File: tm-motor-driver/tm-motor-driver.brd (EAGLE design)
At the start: 47 x 26 mm, 18 parts

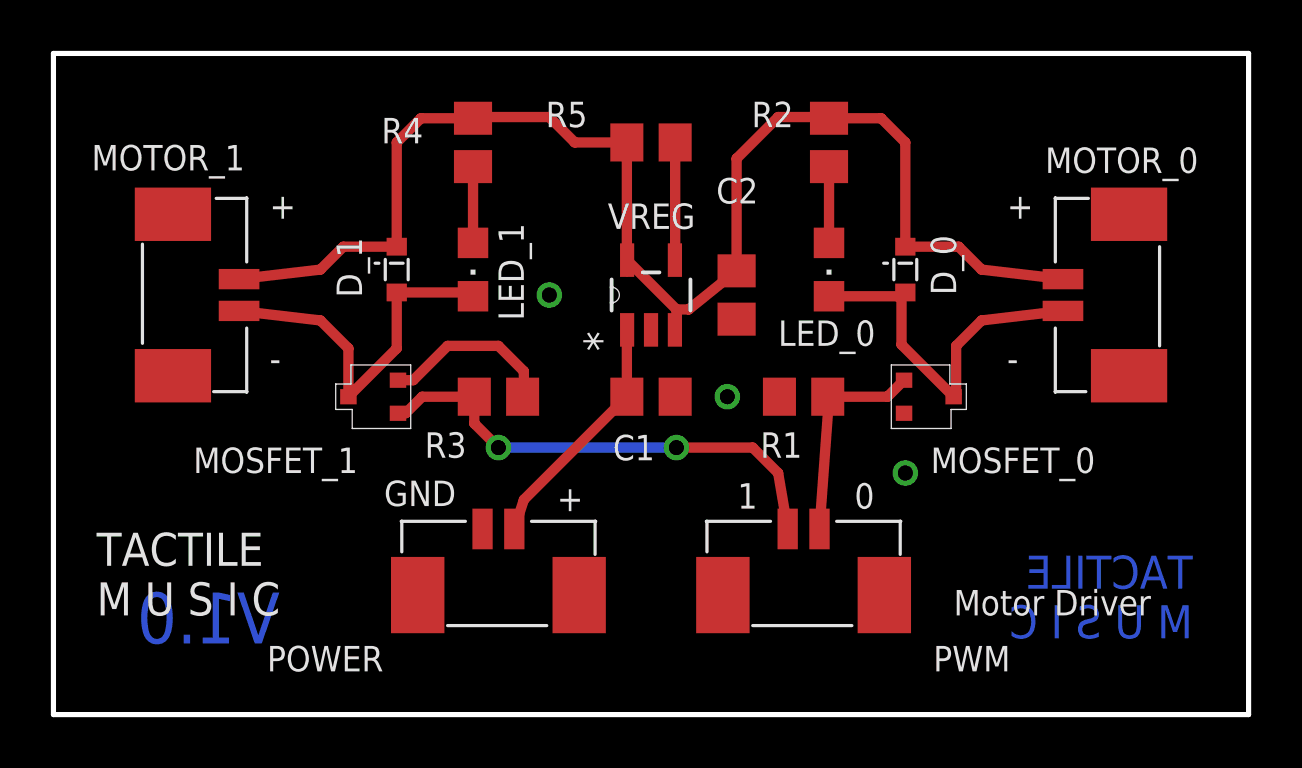
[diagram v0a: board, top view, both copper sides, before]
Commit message: Resize board with new connectors
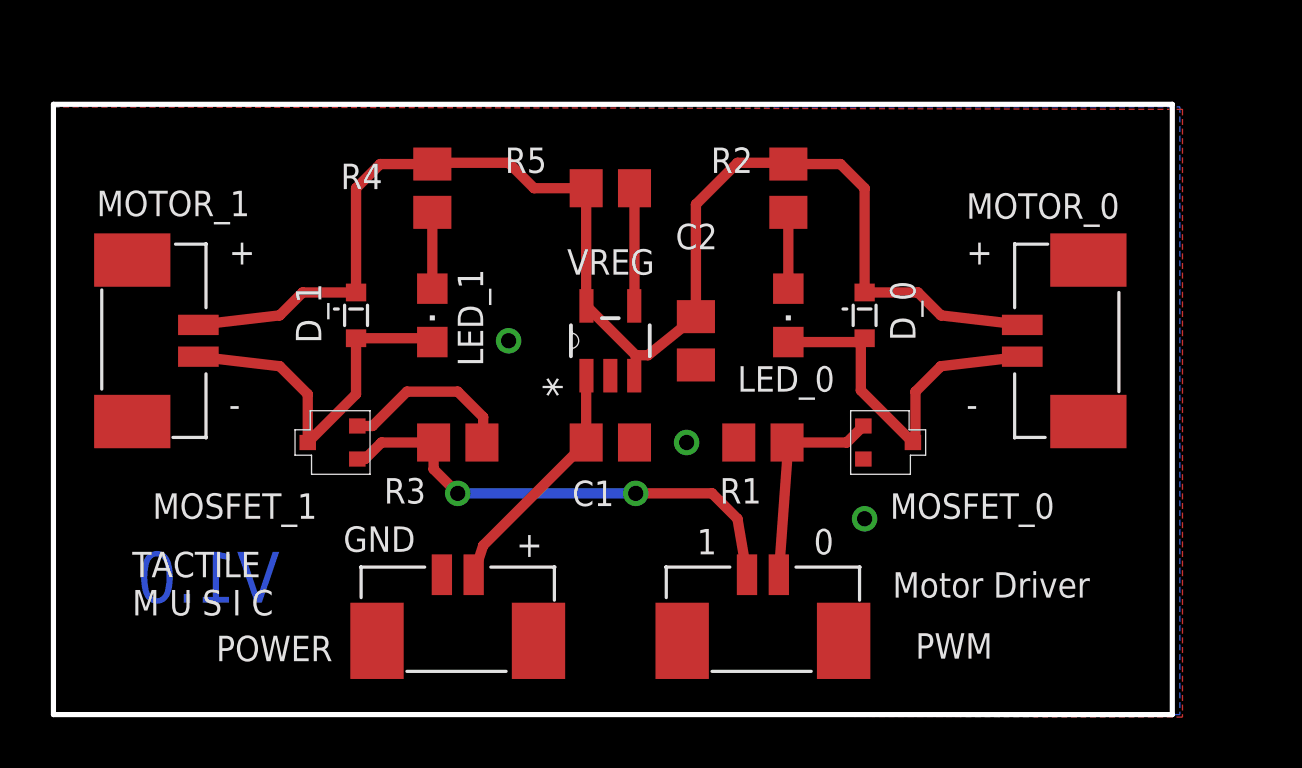
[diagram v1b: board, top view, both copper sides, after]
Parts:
- moved C1 2.41 mm to (21.9, 10.7)
- moved D_0 2.41 mm to (31.9, 15.7)
- moved LED_0 2.41 mm to (28.9, 15.7)
- moved MOSFET_0 2.41 mm to (32.9, 10.7)
- moved MOTOR_0 2.41 mm to (39.9, 14.7)
- moved R1 2.41 mm to (27.9, 10.7)
- moved R2 2.41 mm to (28.9, 20.7)
- moved R5 2.41 mm to (21.9, 20.7)
- moved VREG 2.41 mm to (21.9, 14.7)
- moved PWM 2.41 mm to (27.9, 3.70)
- moved D_1 2.41 mm to (11.9, 15.7)
- moved LED_1 2.41 mm to (14.9, 15.7)
- moved MOSFET_1 2.41 mm to (10.9, 10.7)
- moved MOTOR_1 2.41 mm to (3.90, 14.7)
- moved R3 2.41 mm to (15.9, 10.7)
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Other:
- board size 47 x 26 mm -> 44 x 24 mm

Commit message: Generate gerber files
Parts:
- moved MOTOR_1 1.01 mm to (2.90, 14.6)
- moved POWER 0.72 mm to (15.9, 2.98)
- moved PWM 0.67 mm to (27.9, 3.03)
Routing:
- net +3V3: track 55.0 -> 56.0 mm
- net N$1: track 14.6 -> 15.6 mm
- net BATT_V+: track 9.58 -> 10.3 mm
- net PWM0: track 8.50 -> 9.17 mm
- net PWM1: track 19.3 -> 20.0 mm
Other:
- board size 44 x 24 mm -> 43 x 23.5 mm
- board text added: "C:/EAGLE-7.6.0/lbr/tactile-music-hw-lib/ICON.bmp"
- board text removed: "Motor Driver"
- board text removed: "TACTILE M U S I C"

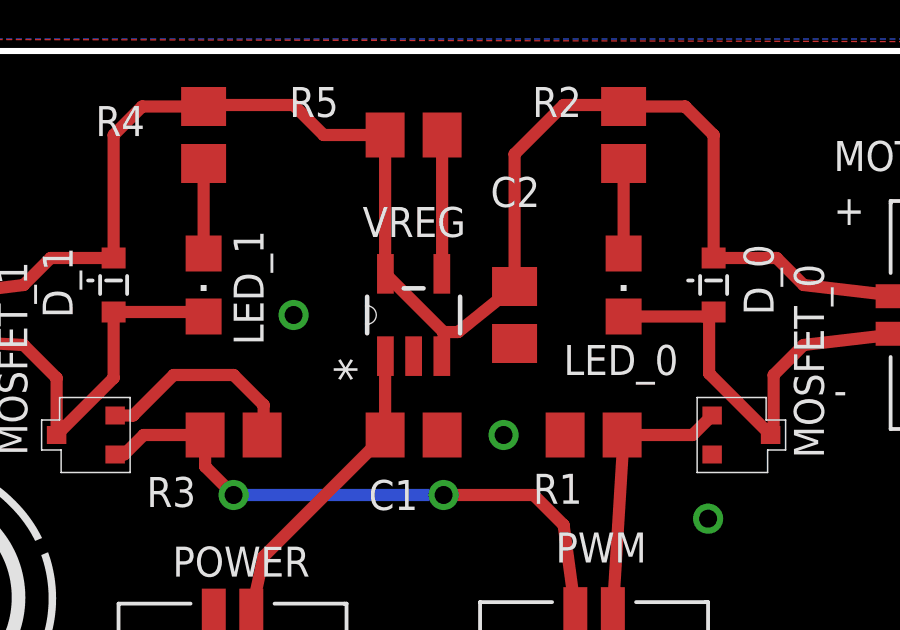
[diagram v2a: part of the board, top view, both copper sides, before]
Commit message: Fix power supply, shutdown should be connected to Vin not Vout
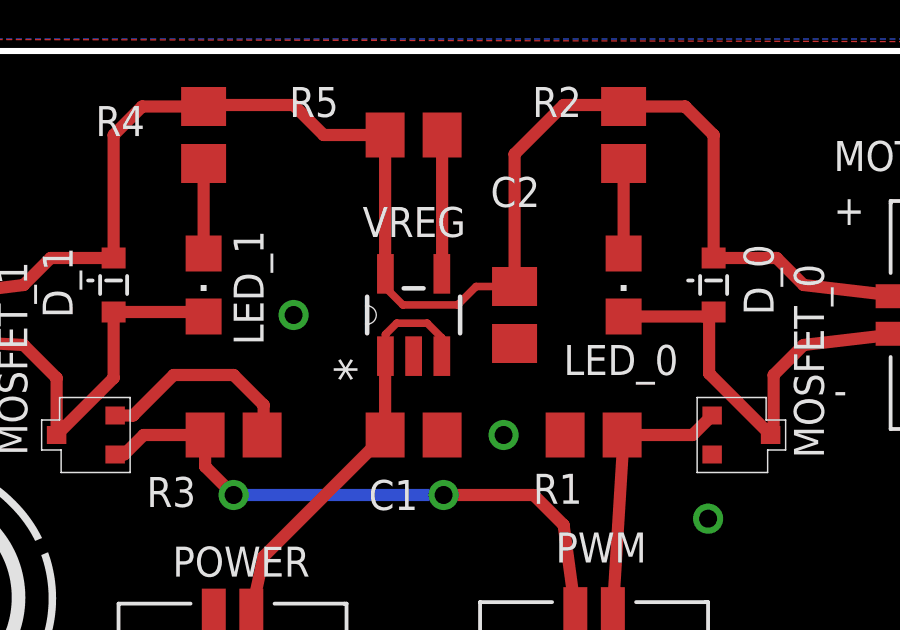
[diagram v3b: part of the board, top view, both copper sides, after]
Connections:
- net +3V3: no longer VREG.3
- net BATT_V+: now also VREG.3
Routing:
- net BATT_V+: track 10.3 -> 13.9 mm
- net +3V3: track 56.0 -> 54.3 mm
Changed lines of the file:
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@@
 <setting verticaltext="up"/>
 </settings>
-<grid distance="0.1" unitdist="mm" unit="mm" style="lines" multiple="1" display="yes" altdistance="0.025" altunitdist="inch" altunit="inch"/>
+<grid distance="8" unitdist="mil" unit="mil" style="lines" multiple="1" display="yes" altdistance="0.025" altunitdist="inch" altunit="inch"/>
 <layers>
 <layer number="1" name="Top" color="4" fill="1" visible="yes" active="yes"/>
@@
 <wire x1="16.489440625" y1="4.778640625" x2="16.9" y2="6.65" width="0.4064" layer="1"/>
 <wire x1="16.9" y1="6.65" x2="20.95" y2="10.7" width="0.4064" layer="1"/>
+<contactref element="VREG" pad="3"/>
+<wire x1="22.8398" y1="13.3284" x2="22.8398" y2="13.9394" width="0.254" layer="1"/>
+<wire x1="22.8398" y1="13.9394" x2="22.352" y2="14.4272" width="0.254" layer="1"/>
+<wire x1="22.352" y1="14.4272" x2="21.336" y2="14.4272" width="0.254" layer="1"/>
+<wire x1="21.336" y1="14.4272" x2="20.9602" y2="14.0514" width="0.254" layer="1"/>
+<wire x1="20.9602" y1="14.0514" x2="20.9602" y2="13.3284" width="0.254" layer="1"/>
 </signal>
 <signal name="PWM0">
@@
 <contactref element="VREG" pad="5"/>
 <contactref element="C2" pad="1"/>
-<contactref element="VREG" pad="3"/>
 <contactref element="R2" pad="2"/>
 <contactref element="R4" pad="2"/>
@@
 <wire x1="9.8" y1="16.6" x2="8.9" y2="15.7" width="0.4064" layer="1"/>
 <wire x1="8.9" y1="15.7" x2="4.704321875" y2="15.17768125" width="0.4064" layer="1"/>
-<wire x1="20.9602" y1="16.0716" x2="20.9602" y2="15.6398" width="0.4064" layer="1"/>
-<wire x1="22.9" y1="13.3886" x2="22.8398" y2="13.3284" width="0.4064" layer="1"/>
-<wire x1="22.9" y1="13.3886" x2="22.9" y2="14.1318" width="0.4064" layer="1"/>
-<wire x1="22.9" y1="14.1318" x2="20.9602" y2="16.0716" width="0.4064" layer="1"/>
 <contactref element="MOTOR_0" pad="2"/>
 <wire x1="28.9" y1="21.65" x2="30.95" y2="21.65" width="0.4064" layer="1"/>
@@
 <wire x1="34" y1="16.6" x2="34.9" y2="15.7" width="0.4064" layer="1"/>
 <wire x1="34.9" y1="15.7" x2="38.1" y2="15.325" width="0.4064" layer="1"/>
-<wire x1="22.9" y1="14.1318" x2="23.3818" y2="14.1318" width="0.4064" layer="1"/>
-<wire x1="23.3818" y1="14.1318" x2="25.265" y2="15.65" width="0.4064" layer="1"/>
 <wire x1="25.265" y1="15.65" x2="25.265" y2="20.065" width="0.4064" layer="1"/>
 <wire x1="25.265" y1="20.065" x2="26.9" y2="21.7" width="0.4064" layer="1"/>
 <wire x1="26.9" y1="21.7" x2="28.85" y2="21.7" width="0.4064" layer="1"/>
 <wire x1="28.85" y1="21.7" x2="28.9" y2="21.65" width="0.4064" layer="1"/>
+<wire x1="25.265" y1="15.65" x2="23.9812" y2="15.65" width="0.254" layer="1"/>
+<wire x1="23.9812" y1="15.65" x2="23.368" y2="15.0368" width="0.254" layer="1"/>
+<wire x1="23.368" y1="15.0368" x2="21.5392" y2="15.0368" width="0.254" layer="1"/>
+<wire x1="21.5392" y1="15.0368" x2="20.9602" y2="15.6158" width="0.254" layer="1"/>
+<wire x1="20.9602" y1="15.6158" x2="20.9602" y2="16.0716" width="0.254" layer="1"/>
 </signal>
 <signal name="N$2">
